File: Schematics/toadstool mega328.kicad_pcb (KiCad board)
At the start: 2 copper layers, 49.5 x 81.2 mm, 26 parts, among them CON1 BARREL_JACK, IC1 ATMEGA328P-P, K1 CAP, K2 V-SELECT, K4 ICSP, K5 PIN 2-8, K6 PIN 21-28, K7 XTAL, K8 PIN 15-19, K9 PIN 11-14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

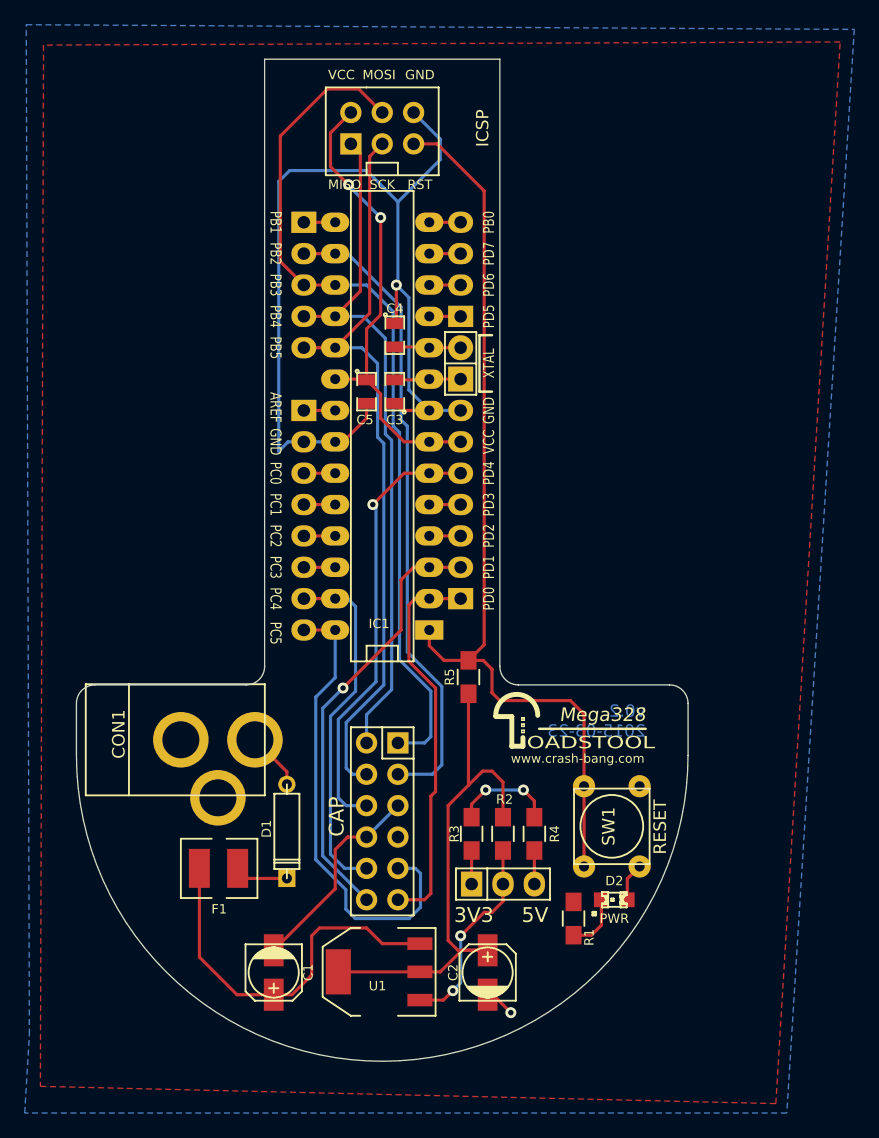
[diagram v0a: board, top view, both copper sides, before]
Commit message: Cap Header
Widening of Cap Header
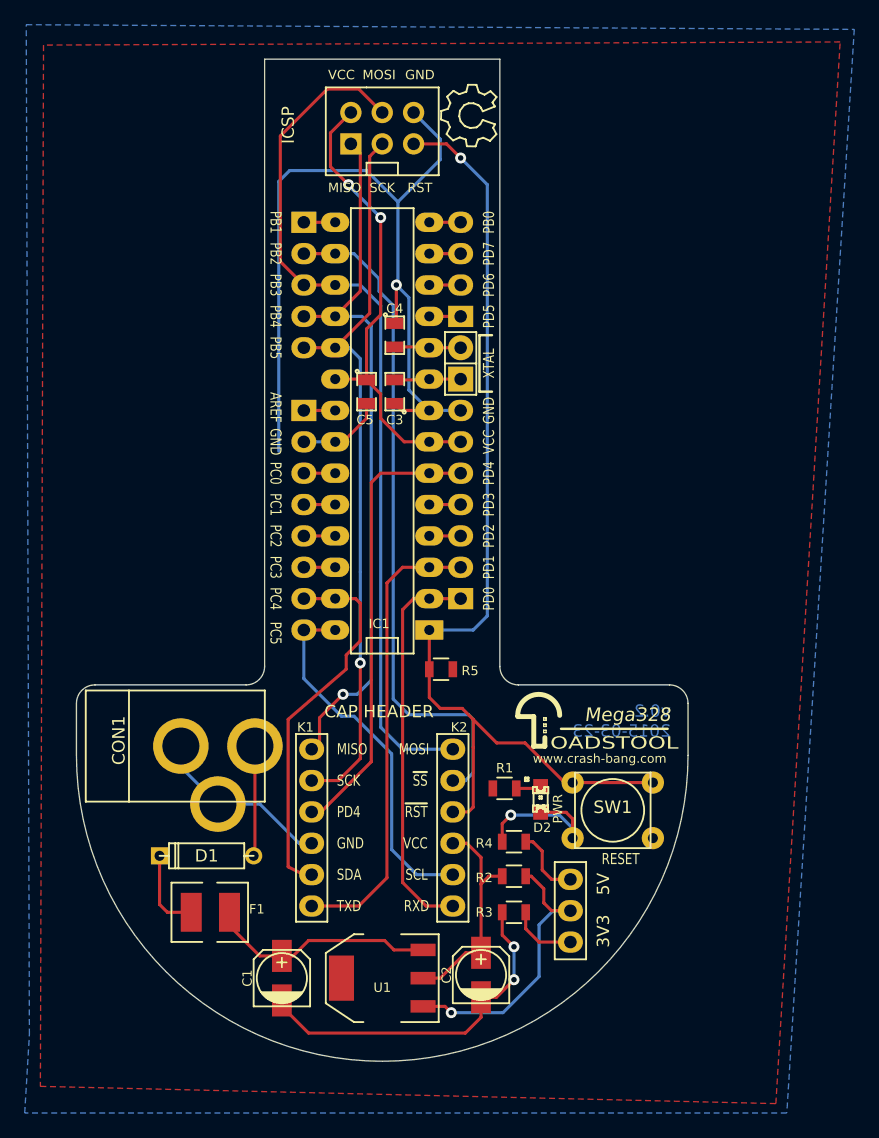
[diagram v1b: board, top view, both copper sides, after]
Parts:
- added K3: V-SELECT, Pin_Header_Straight_1x03, F.Cu at (223.5, 119.3)
- added REF**: Symbol_OSHW-Logo_SilkScreen, Toadstool:Symbol_OSHW-Logo_SilkScreen, F.Cu at (215.5, 52.3)
- C1: footprint toadstool:c_elec_4x5.3 -> Toadstool:c_elec_4x5.3
- D1: footprint Discret:D3 -> Toadstool:Diode_D3
- IC1: footprint Sockets_DIP:DIP-28__300_ELL -> ATMEGA328P-P
- K1: value CAP -> CAP_CONN_LHS; footprint Socket_Strips:Socket_Strip_Straight_2x06 -> Toadstool:Socket_Strip_Straight_1x06
- K2: value V-SELECT -> CAP_CONN_RHS; footprint Pin_Headers:Pin_Header_Straight_1x03 -> Toadstool:Socket_Strip_Straight_1x06
- R1: value R -> R330; footprint Resistors_SMD:R_0805_HandSoldering -> Resistors_SMD:R_0805
- R2, R3, R4, R5: footprint Resistors_SMD:R_0805_HandSoldering -> Resistors_SMD:R_0805
- U1: footprint SOT-223 -> Toadstool:SOT-223
- moved R1 11.9 mm to (218.2, 106.8), turned to 180 degrees
- moved K2 11.7 mm to (214.0, 103.6), turned to 270 degrees
- moved D2 10.1 mm to (221.1, 107.7), turned to 270 degrees
- moved K1 8.17 mm to (202.6, 103.6), turned to 270 degrees
- moved R3 7.22 mm to (218.9, 116.8), turned to 0 degrees
- moved D1 6.80 mm to (194.1, 112.3), turned to 180 degrees
- moved F1 3.64 mm to (194.3, 116.8), turned to 180 degrees
- moved R2 3.54 mm to (218.9, 113.9), turned to 180 degrees
- moved R5 2.31 mm to (213.0, 97.2), turned to 0 degrees
- moved Toadstool_Logo 1.78 mm to (225.6, 101.1)
- moved R4 1.77 mm to (218.9, 111.1), turned to 0 degrees
- moved SW1 1.30 mm to (226.9, 108.6), turned to 0 degrees
- moved C1 0.80 mm to (200.2, 122.2), turned to 90 degrees
- moved C2 0.57 mm to (216.3, 121.9)
- moved U1 0.57 mm to (208.3, 122.2)
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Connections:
- K1 pad 1: /PB3 -> /PB4
- K1 pad 2: /PB4 -> /PB5
- K1 pad 3: /PB2 -> /PD4
- K1 pad 4: /PB5 -> GND
- K1 pad 5: GND -> /PC4
- K1 pad 6: /PD4 -> /PD1
- K2 pad 1: Net-(K2-Pad1) -> /PB3
- K2 pad 2: Net-(K2-Pad2) -> /PB2
- K2 pad 3: Net-(K2-Pad3) -> /RST
- R2 pad 1: Net-(K2-Pad2) -> Net-(K3-Pad2)
- R3 pad 2: Net-(K2-Pad1) -> Net-(K3-Pad1)
- R4 pad 2: Net-(K2-Pad3) -> Net-(K3-Pad3)
- U1 pad 1: Net-(K2-Pad2) -> Net-(K3-Pad2)
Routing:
- net VCC: track 82.5 -> 56.9 mm
- net GND: track 109.5 -> 134.1 mm
- net Net-(K3-Pad2): track 0.00 -> 23.5 mm, vias 0 -> 1
- net Net-(K2-Pad2): track 16.9 -> 0.00 mm, vias 2 -> 0
- net Net-(C1-Pad1): track 30.9 -> 18.6 mm
- net /PC5: track 38.3 -> 29.0 mm
- net /RST: track 75.4 -> 83.4 mm, vias 0 -> 1
- net Net-(K3-Pad3): track 0.00 -> 5.78 mm
- net Net-(K3-Pad1): track 0.00 -> 5.40 mm
- net /PB2: track 52.0 -> 56.5 mm
- net Net-(CON1-Pad1): track 4.68 -> 8.93 mm
- net /PC4: track 29.5 -> 33.2 mm
- net Net-(D2-Pad1): track 4.97 -> 2.04 mm
- net Net-(K2-Pad3): track 2.71 -> 0.00 mm
- net Net-(K2-Pad1): track 2.71 -> 0.00 mm
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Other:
- board text added: "CAP HEADER"
- board text added: "RXD"
- board text added: "SCL"
- board text added: "SDA"
- board text added: "TXD"
- board text added: "~RST"
- board text added: "~SS"

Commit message: Final Prototype Commit
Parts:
- C2: footprint toadstool:c_elec_4x5.3 -> Toadstool:c_elec_4x5.3
- C3, C4, C5: footprint SMD_Packages:SMD-0805 -> Capacitors_SMD:C_0805_HandSoldering
- CON1: footprint toadstool:BARREL_JACK_No_Slot -> Toadstool:BARREL_JACK_No_Slot
- F1: footprint toadstool:MiniSMDPTC-4532 -> Toadstool:MiniSMDPTC-4532
- K3: footprint Pin_Header_Straight_1x03 -> Toadstool:Pin_Header_Straight_1x03
- R1, R2, R3, R4, R5: footprint Resistors_SMD:R_0805 -> Resistors_SMD:R_0805_HandSoldering
- SW1: footprint toadstool:SW_PUSH -> Toadstool:Switch_SMT_Alps_SKQGAxE010
- moved C4 0.25 mm to (209.3, 69.8)
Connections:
- net Net-(K3-Pad1) renamed /3.3V
- net Net-(K3-Pad3) renamed /5V
- K1 pad 3: /PD4 -> /PD3
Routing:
- net /PD4: track 36.0 -> 2.54 mm
- net /PD3: track 2.54 -> 33.3 mm
- net GND: track 134.1 -> 135.7 mm
- net /RST: track 83.4 -> 82.7 mm
- net /5V: track 5.78 -> 5.06 mm
- net Net-(K3-Pad2): track 23.5 -> 22.8 mm
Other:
- board text added: "v0.3 2015-04-26"
- board text removed: "v0.2 2015-03-23"

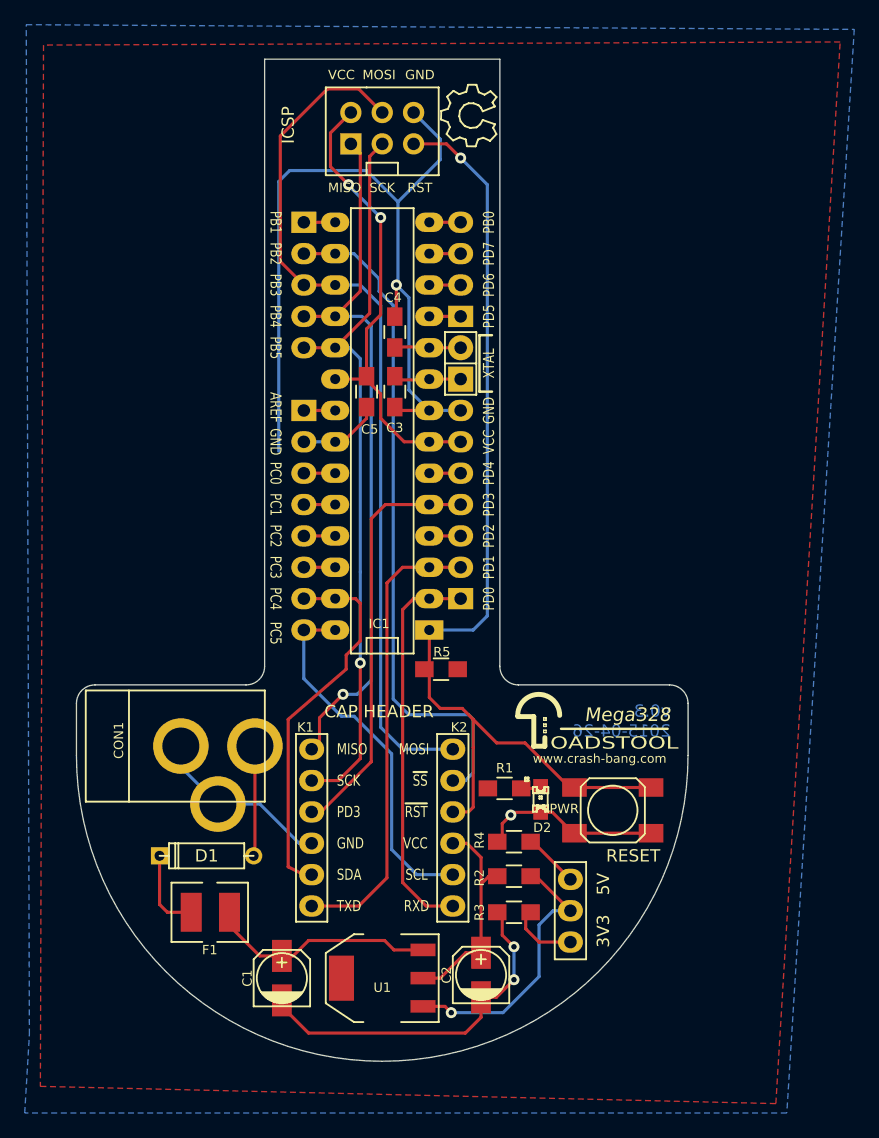
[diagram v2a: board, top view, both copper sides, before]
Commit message: Cosmetic Changes to Silkscreen
Cosmetic Changes to Silkscreen
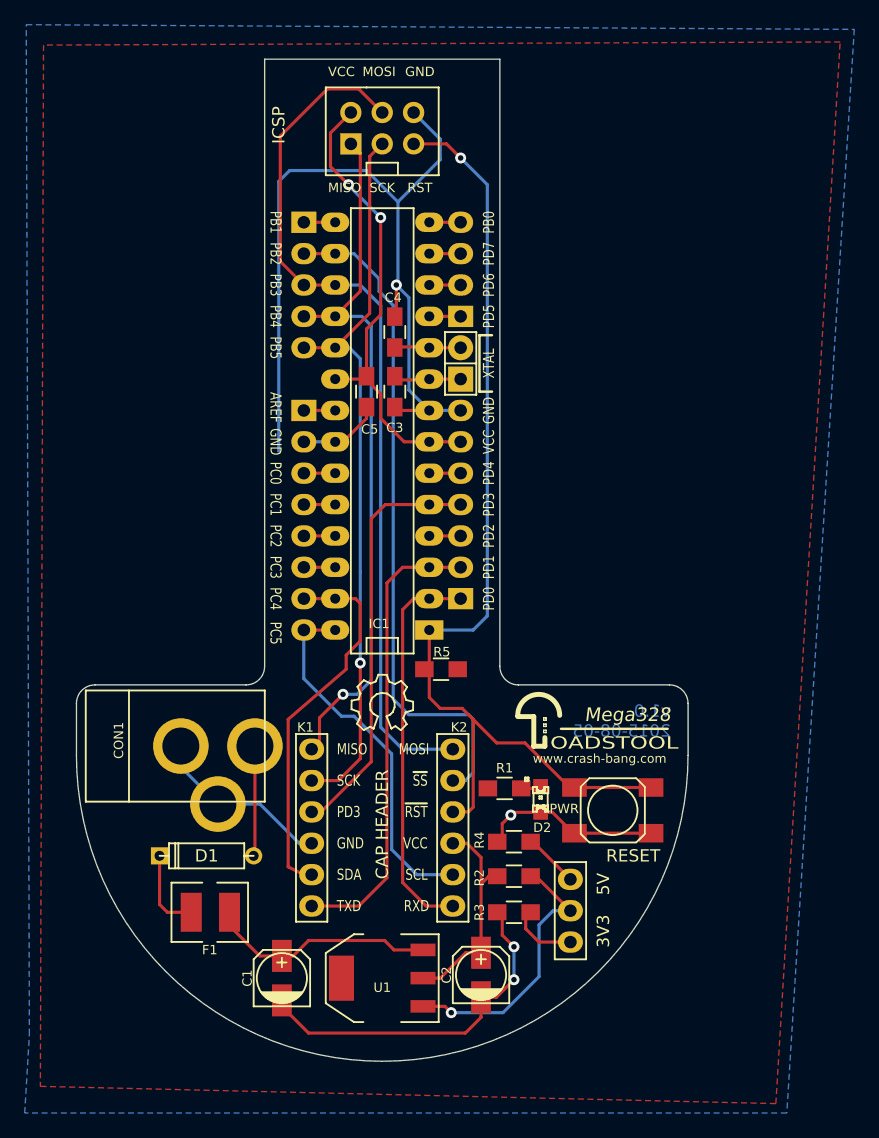
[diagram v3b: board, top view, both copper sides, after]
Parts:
- moved REF** 48.3 mm to (208.3, 100.1), turned to 0 degrees
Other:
- board text added: "v1.0 2015-08-05"
- board text removed: "v0.3 2015-04-26"
